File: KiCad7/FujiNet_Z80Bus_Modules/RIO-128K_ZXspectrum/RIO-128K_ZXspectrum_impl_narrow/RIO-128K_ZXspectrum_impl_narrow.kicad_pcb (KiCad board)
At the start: 2 copper layers, 45 x 95 mm, 8 parts, among them J1 Conn_01x24_Socket, J2 Conn_01x18_Socket

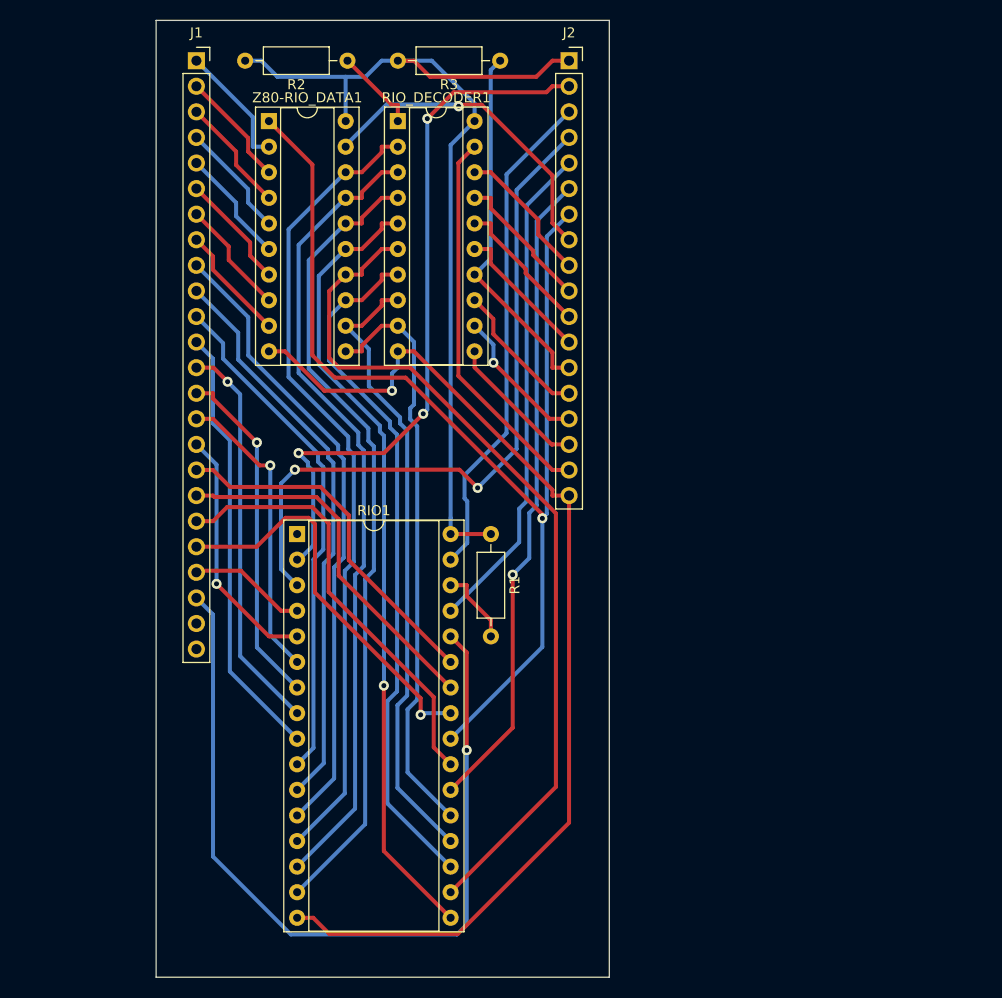
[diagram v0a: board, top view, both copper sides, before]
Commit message: KiCad Corrected the orientation of the impl PCBs
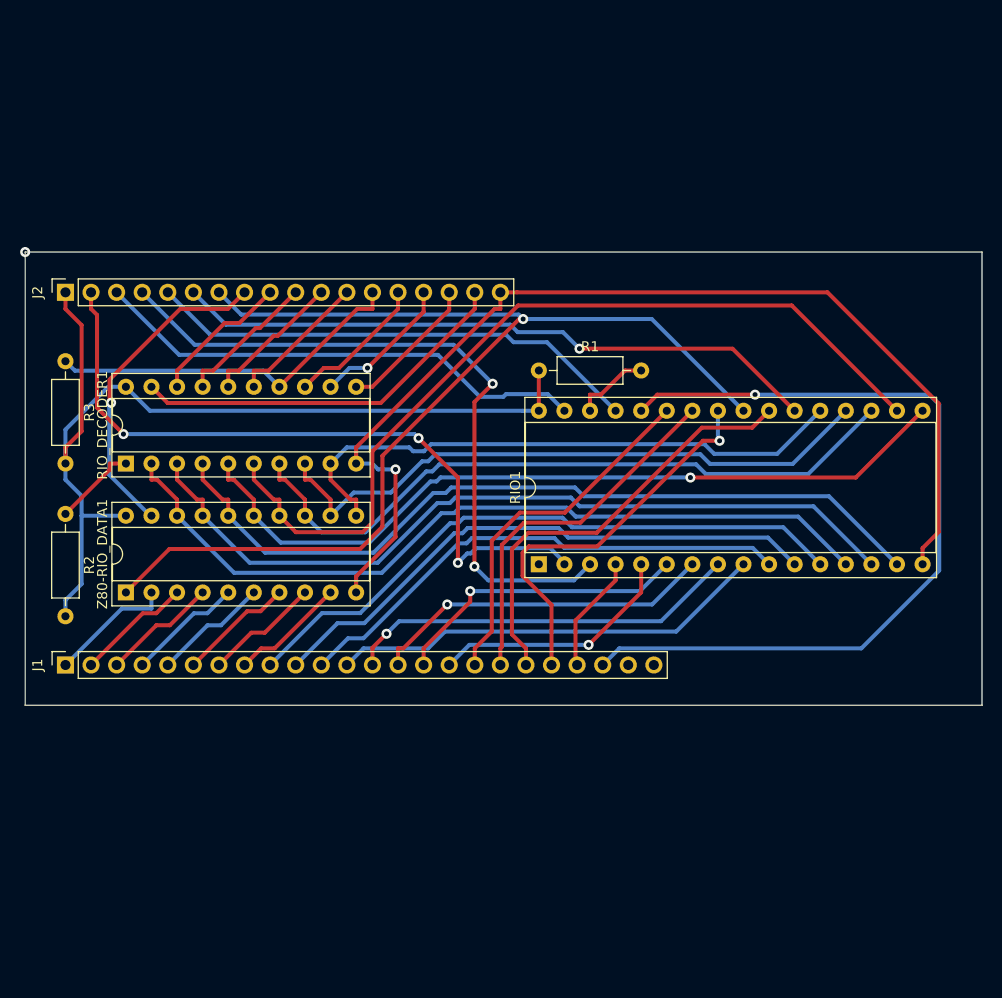
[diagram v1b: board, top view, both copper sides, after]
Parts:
- moved J1 61.4 mm to (102.0, 130.0), turned to 90 degrees
- moved J2 55.0 mm to (102.0, 93.0), turned to 90 degrees
- moved R2 53.0 mm to (102.0, 115.0), turned to -90 degrees
- moved R3 52.5 mm to (102.0, 99.8), turned to -90 degrees
- moved Z80-RIO_DATA1 48.9 mm to (108.0, 122.8), turned to 90 degrees
- moved RIO_DECODER1 43.4 mm to (108.0, 110.0), turned to 90 degrees
- moved RIO1 24.2 mm to (149.0, 120.0), turned to 90 degrees
- moved R1 16.9 mm to (149.0, 100.8), turned to 0 degrees
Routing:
- net (no net): vias 0 -> 1
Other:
- board size 45 x 95 mm -> 95 x 45 mm
